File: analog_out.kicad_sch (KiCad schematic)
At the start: 13 parts, among them U24 TSB582

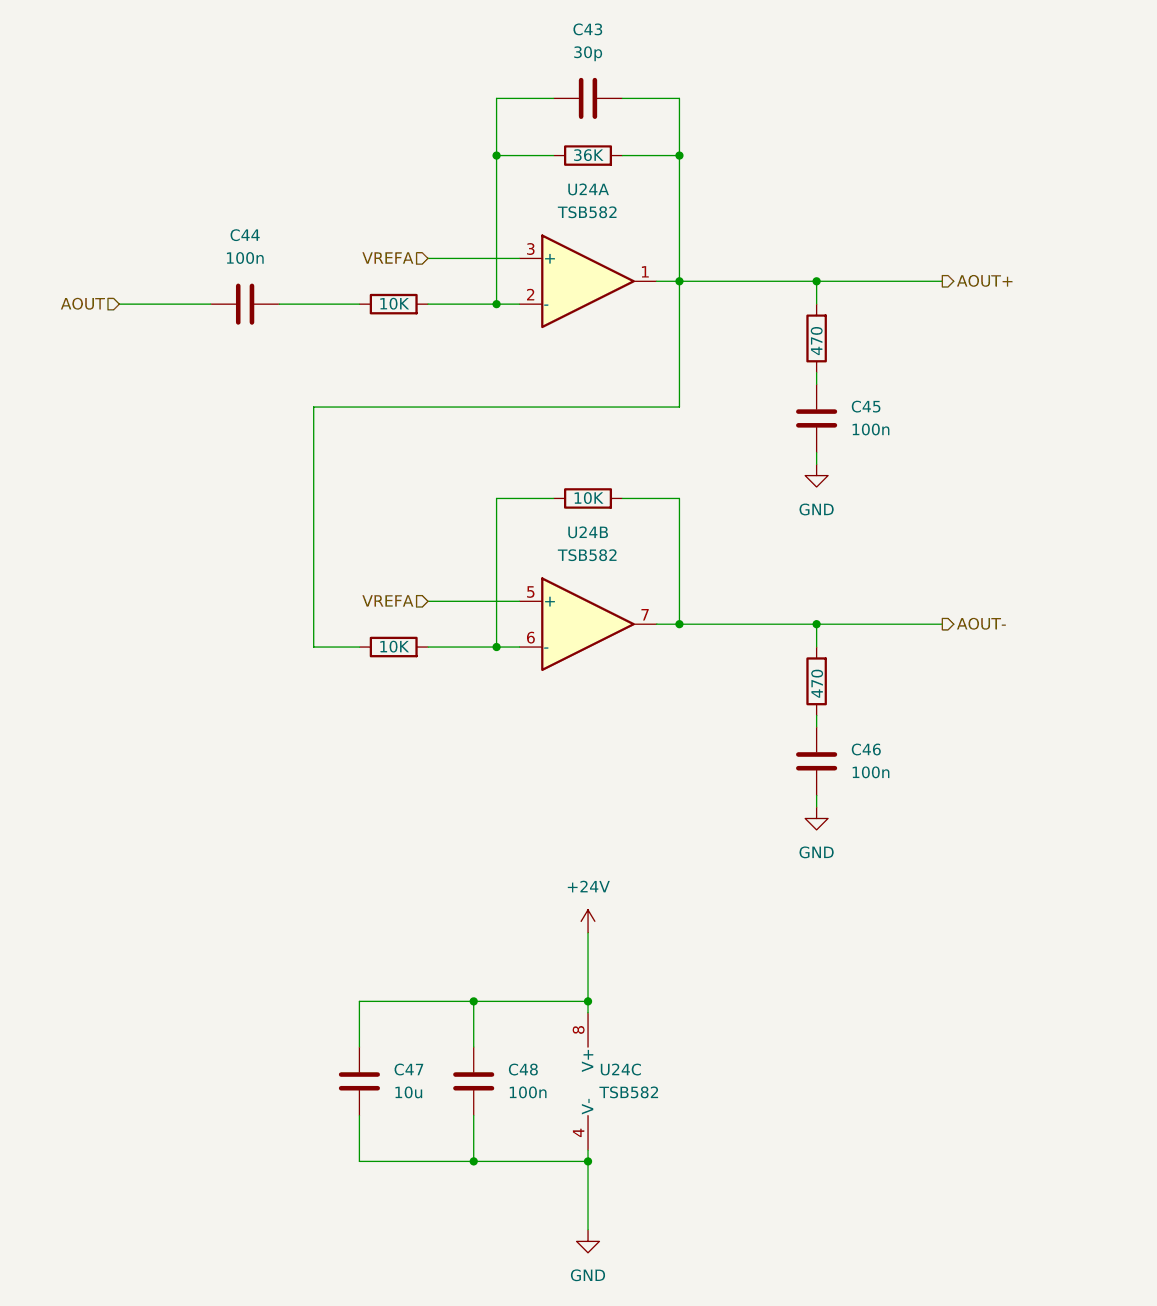
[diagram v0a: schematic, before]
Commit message: Assigned footprints for analog circuit
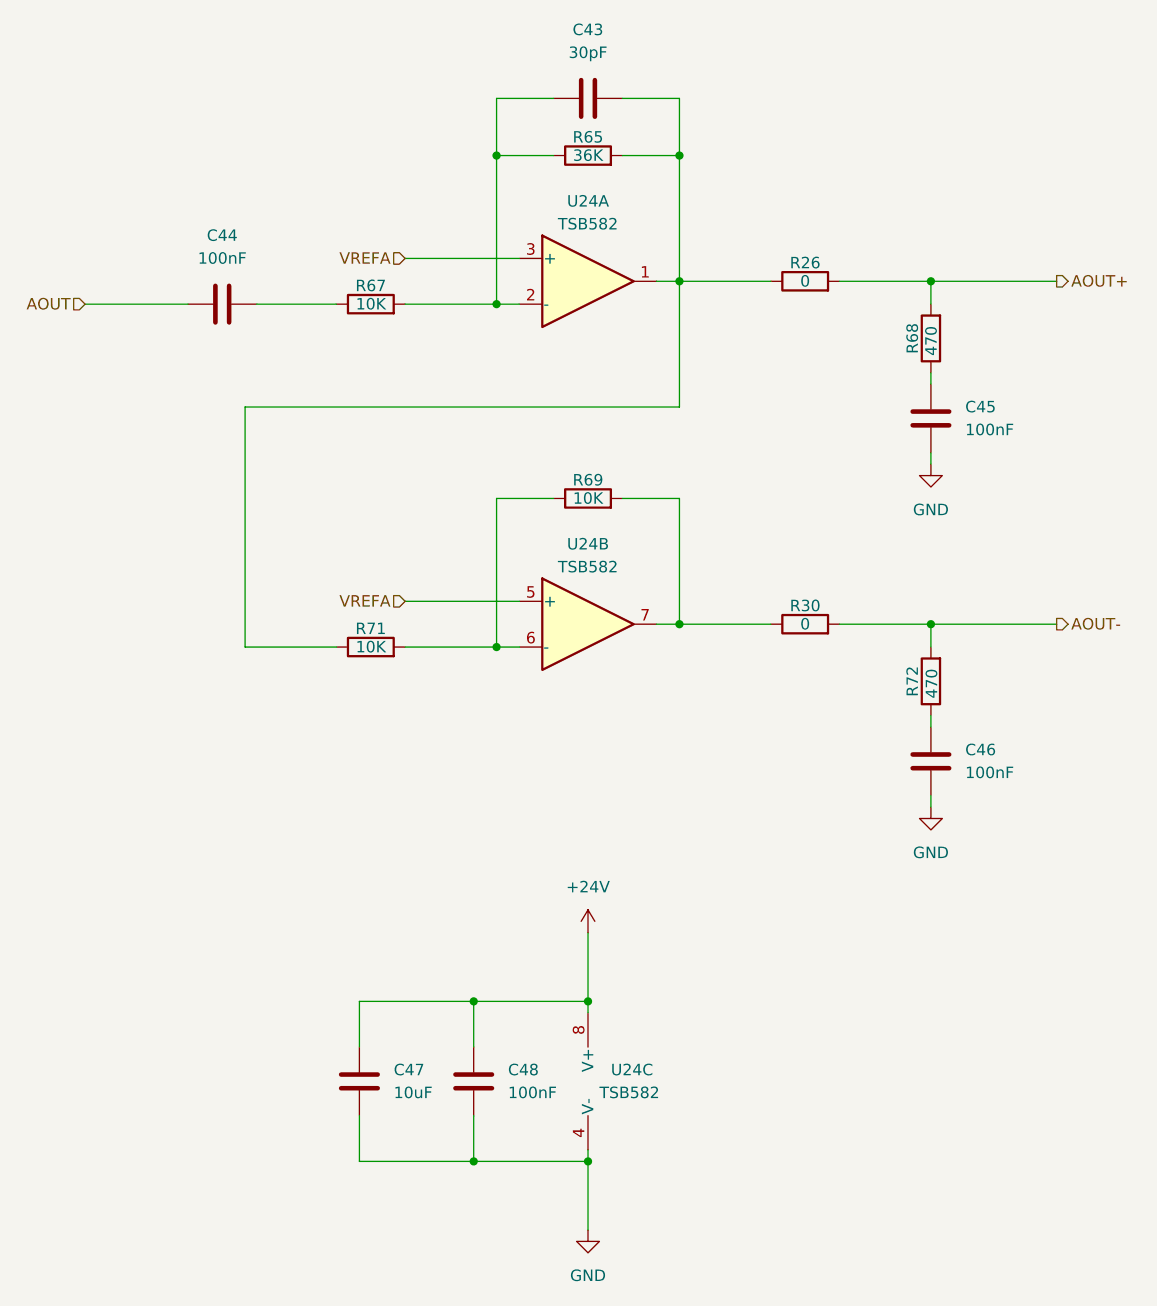
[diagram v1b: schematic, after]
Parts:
- added R26, R30: 0, Resistor_SMD:R_0603_1608Metric_Pad0.98x0.95mm_HandSolder, symbol Device:R
- C43: value 30p -> 30pF
- C44, C45, C46, C48: value 100n -> 100nF
- C47: value 10u -> 10uF
- renumbered R55 to R65, R56 to R67, R57 to R68, R58 to R69, R59 to R71, R60 to R72
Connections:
- net AOUT+: now also R26.2; no longer C43.2, R65.2, R71.1, U24.1
- net AOUT-: now also R30.2; no longer R69.2, U24.7
- new net: C43.2, R26.1, R65.2, R71.1, U24.1
- new net: R30.1, R69.2, U24.7
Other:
- moved on the sheet: C44, C45, C46

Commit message: Updated files to kicad 10
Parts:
- renumbered C43 to C13, C44 to C14, C45 to C15, C46 to C16, C47 to C17, C48 to C18, R65 to R25, R67 to R27, R68 to R28, R69 to R29, R71 to R31, R72 to R32, U24 to U19
